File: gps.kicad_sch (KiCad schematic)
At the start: 10 parts, among them J700 Conn_01x02, U700 NEO-6P, X7 Conn_Coaxial

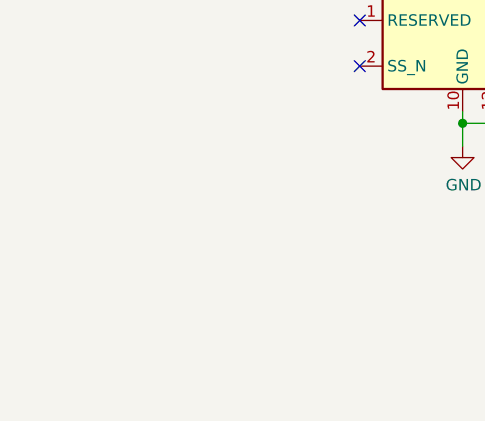
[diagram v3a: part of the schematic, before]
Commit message: Changed the position of the capacitor in the circuit diagram. Capacitors are now close to the components as on the circuit board.
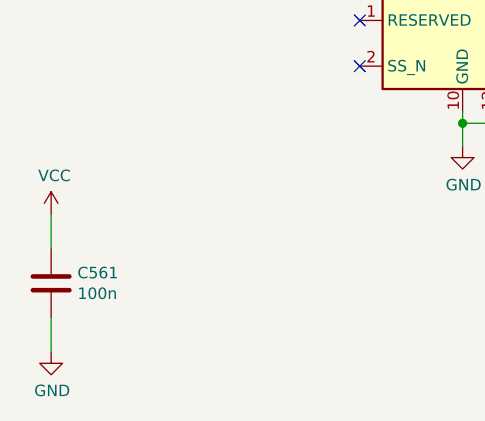
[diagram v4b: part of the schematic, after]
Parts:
- added C561: 100n, Capacitor_SMD:C_0805_2012Metric_Pad1.18x1.45mm_HandSolder, symbol Device:C
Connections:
- net GND: now also C561.2
- net VCC: now also C561.1
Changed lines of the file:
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@@
   (no_connect (at 163.83 91.44))
   (no_connect (at 163.83 101.6))
+  (wire (pts (xy 93.98 121.92) (xy 93.98 125.73))
+    (stroke (width 0) (type solid) (color 0 0 0 0))
+  )
+  (wire (pts (xy 93.98 133.35) (xy 93.98 137.16))
+    (stroke (width 0) (type solid) (color 0 0 0 0))
+  )
   (wire (pts (xy 102.87 80.01) (xy 109.22 80.01))
     (stroke (width 0) (type solid) (color 0 0 0 0))
@@
     )
   )
+  (symbol (lib_id "power:VCC") (at 93.98 121.92 0) (unit 1)
+    (in_bom yes) (on_board yes)
+    (property "Reference" "#PWR0202" (id 0) (at 93.98 125.73 0)
+      (effects (font (size 1.27 1.27)) hide)
+    )
+    (property "Value" "VCC" (id 1) (at 94.3483 117.5956 0))
+    (property "Footprint" "" (id 2) (at 93.98 121.92 0)
+      (effects (font (size 1.27 1.27)) hide)
+    )
+    (property "Datasheet" "" (id 3) (at 93.98 121.92 0)
+      (effects (font (size 1.27 1.27)) hide)
+    )
+    (pin "1")
+  )
   (symbol (lib_id "power:VCC") (at 142.24 60.96 0) (unit 1)
     (in_bom yes) (on_board yes)
@@
     (pin "1")
   )
+  (symbol (lib_id "power:GND") (at 93.98 137.16 0) (unit 1)
+    (in_bom yes) (on_board yes)
+    (property "Reference" "#PWR0201" (id 0) (at 93.98 143.51 0)
+      (effects (font (size 1.27 1.27)) hide)
+    )
+    (property "Value" "GND" (id 1) (at 94.0943 141.4844 0))
+    (property "Footprint" "" (id 2) (at 93.98 137.16 0)
+      (effects (font (size 1.27 1.27)) hide)
+    )
+    (property "Datasheet" "" (id 3) (at 93.98 137.16 0)
+      (effects (font (size 1.27 1.27)) hide)
+    )
+    (pin "1")
+  )
   (symbol (lib_id "power:GND") (at 139.7 114.3 0) (unit 1)
     (in_bom yes) (on_board yes)
@@
       (effects (font (size 1.27 1.27)) hide)
     )
+    (pin "1")
+    (pin "2")
+  )
+  (symbol (lib_id "Device:C") (at 93.98 129.54 0) (unit 1)
+    (in_bom yes) (on_board yes)
+    (property "Reference" "C561" (id 0) (at 96.9011 128.3906 0)
+      (effects (font (size 1.27 1.27)) (justify left))
+    )
+    (property "Value" "100n" (id 1) (at 96.9011 130.6893 0)
+      (effects (font (size 1.27 1.27)) (justify left))
+    )
+    (property "Footprint" "Capacitor_SMD:C_0805_2012Metric_Pad1.18x1.45mm_HandSolder" (id 2) (at 94.9452 133.35 0)
+      (effects (font (size 1.27 1.27)) hide)
+    )
+    (property "Datasheet" "~" (id 3) (at 93.98 129.54 0)
+      (effects (font (size 1.27 1.27)) hide)
+    )
+    (property "JLCBasicPart" "Basic" (id 4) (at 93.98 129.54 0)
+      (effects (font (size 1.27 1.27)) hide)
+    )
+    (property "JLCPartNr" "C49678" (id 5) (at 93.98 129.54 0)
+      (effects (font (size 1.27 1.27)) hide)
+    )
+    (property "JLCType" "CC0805KRX7R9BB104" (id 6) (at 93.98 129.54 0)
+      (effects (font (size 1.27 1.27)) hide)
+    )
+    (property "OriginalType" "FN21X104K500PXG " (id 7) (at 93.98 129.54 0)
+      (effects (font (size 1.27 1.27)) hide)
+    )

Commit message: Progress in PCB. Some changes in Schematis. Solderjumper for modular design added.
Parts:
- X7: footprint muonpi-kicad-library:SMA_Samtec_SMA-J-P-X-ST-EM1_EdgeMount -> muonpi-kicad-library:Connector_Coaxial_SMA_edge_combined
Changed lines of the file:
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@@
       (effects (font (size 1.27 1.27)) (justify left))
     )
-    (property "Footprint" "muonpi-kicad-library:SMA_Samtec_SMA-J-P-X-ST-EM1_EdgeMount" (id 2) (at 176.53 80.01 0)
+    (property "Footprint" "muonpi-kicad-library:Connector_Coaxial_SMA_edge_combined" (id 2) (at 176.53 80.01 0)
       (effects (font (size 1.27 1.27)) hide)
     )

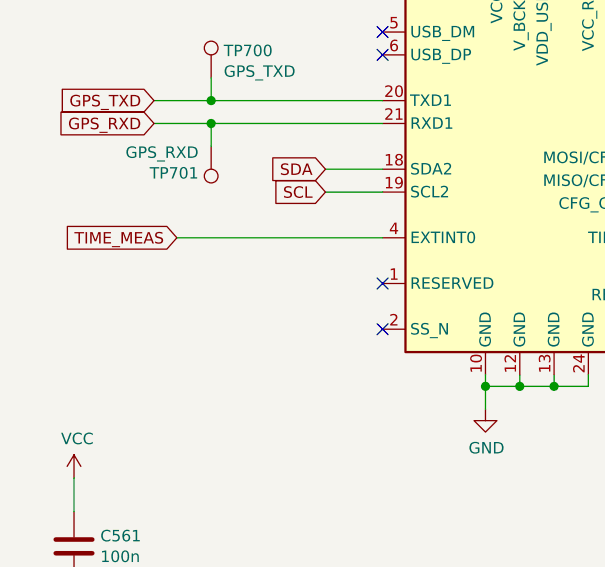
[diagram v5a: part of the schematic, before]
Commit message: Removed optionals parts. Cleaned up Schematics
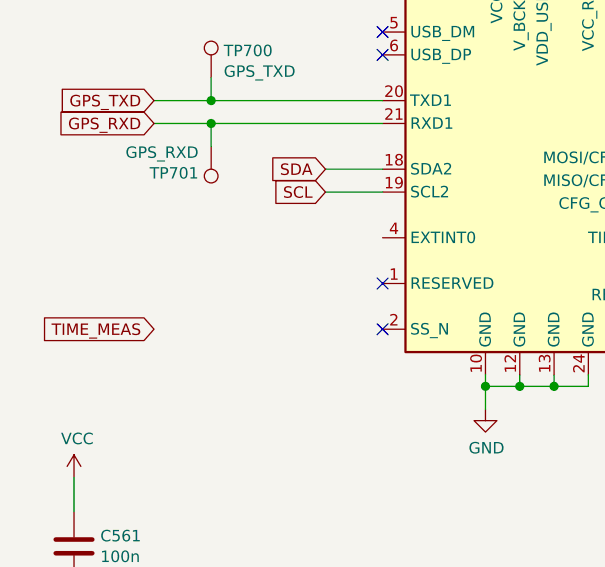
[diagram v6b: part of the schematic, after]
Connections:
- net TIME_MEAS: no longer U700.4 (EXTINT0)
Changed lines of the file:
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@@
-    (stroke (width 0) (type solid) (color 0 0 0 0))
-  )
-  (wire (pts (xy 105.41 95.25) (xy 128.27 95.25))
     (stroke (width 0) (type solid) (color 0 0 0 0))
   )
@@
     )
   )
-  (global_label "TIME_MEAS" (shape input) (at 105.41 95.25 180)
+  (global_label "TIME_MEAS" (shape input) (at 102.87 105.41 180)
     (effects (font (size 1.27 1.27)) (justify right))
-    (property "Intersheet References" "${INTERSHEET_REFS}" (id 0) (at 91.4339 95.1706 0)
+    (property "Intersheet References" "${INTERSHEET_REFS}" (id 0) (at 88.8939 105.3306 0)
       (effects (font (size 1.27 1.27)) (justify right) hide)
     )

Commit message: Rough routing finished
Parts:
- added JP700, JP701, JP702, JP703, JP704, JP705: SolderJumper_2_Bridged, Jumper:SolderJumper-2_P1.3mm_Bridged_Pad1.0x1.5mm, symbol Jumper:SolderJumper_2_Bridged
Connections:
- net GPS_RXD: now also JP701.1 (A); no longer TP701.1, U700.21 (RXD1)
- net GPS_TXD: now also JP700.1 (A); no longer TP700.1, U700.20 (TXD1)
- net SCL: now also JP703.1 (A); no longer U700.19 (SCL2)
- net SDA: now also JP702.1 (A); no longer U700.18 (SDA2)
- net TIMEPULSE: now also JP704.2 (B); no longer R705.2
- net TIME_MEAS: now also JP705.1 (A)
- net at U700.4 (EXTINT0): now also JP705.2 (B)
- new net: JP702.2 (B), U700.18 (SDA2)
- new net: JP703.2 (B), U700.19 (SCL2)
- new net: JP700.2 (B), TP700.1, U700.20 (TXD1)
- new net: JP701.2 (B), TP701.1, U700.21 (RXD1)
- new net TIMEPULSE_LED: JP704.1 (A), R705.2

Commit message: some changes after first test of boards. Package of SN74LV221AD changed to SOIC-16.
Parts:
- C561: JLCplace (none) -> C49678; Supplier (none) -> LCSC
- J700: OriginalType (none) -> 67997-100HLF; Supplier (none) -> Mouser
- JP700, JP701, JP702, JP703, JP704, JP705, TP700, TP701: Supplier (none) -> --
- L700: alternativ supply (none) -> mouser; alternativ supply part nr. (none) -> CE201210-27NJ
- R700: JLCplace (none) -> C17415; Supplier (none) -> LCSC
- R704: JLCplace (none) -> C17477; Supplier (none) -> LCSC
- R705, R706: JLCplace (none) -> C17738; Supplier (none) -> LCSC
- U700: Supplier (none) -> ??
- X7: JLCBasicPart (none) -> Extended; JLCPartNr (none) -> C88374; JLCType (none) -> U.FL-R-SMT-1(80); OriginalType (none) -> U.FL-R-SMT-1(80); Supplier (none) -> LCSC
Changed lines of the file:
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@@
+      (effects (font (size 1.27 1.27)) hide)
+    )
+    (property "Supplier" "--" (id 4) (at 109.22 77.47 0)
       (effects (font (size 1.27 1.27)) hide)
     )
@@
     )
     (property "Datasheet" "~" (id 3) (at 104.14 85.09 0)
+      (effects (font (size 1.27 1.27)) hide)
+    )
+    (property "Supplier" "--" (id 4) (at 109.22 85.09 0)
       (effects (font (size 1.27 1.27)) hide)
     )
@@
       (effects (font (size 1.27 1.27)) hide)
     )
+    (property "alternativ supply" "mouser" (id 9) (at 170.18 74.93 0)
+      (effects (font (size 1.27 1.27)) hide)
+    )
+    (property "alternativ supply part nr." "CE201210-27NJ" (id 10) (at 170.18 74.93 0)
+      (effects (font (size 1.27 1.27)) hide)
+    )
     (pin "1")
     (pin "2")
@@
       (effects (font (size 1.27 1.27)) hide)
     )
+    (property "Supplier" "--" (id 4) (at 102.87 80.01 0)
+      (effects (font (size 1.27 1.27)) hide)
+    )
     (pin "1")
     (pin "2")
@@
       (effects (font (size 1.27 1.27)) hide)
     )
+    (property "Supplier" "--" (id 4) (at 102.87 82.55 0)
+      (effects (font (size 1.27 1.27)) hide)
+    )
     (pin "1")
     (pin "2")
@@
       (effects (font (size 1.27 1.27)) hide)
     )
+    (property "Supplier" "--" (id 4) (at 120.65 97.79 0)
+      (effects (font (size 1.27 1.27)) hide)
+    )
     (pin "1")
     (pin "2")
@@
       (effects (font (size 1.27 1.27)) hide)
     )
+    (property "Supplier" "--" (id 4) (at 123.19 87.63 0)
+      (effects (font (size 1.27 1.27)) hide)
+    )
     (pin "1")
     (pin "2")
@@
       (effects (font (size 1.27 1.27)) hide)
     )
+    (property "Supplier" "--" (id 4) (at 123.19 90.17 0)
+      (effects (font (size 1.27 1.27)) hide)
+    )
     (pin "1")
     (pin "2")
@@
       (effects (font (size 1.27 1.27)) hide)
     )
+    (property "Supplier" "--" (id 4) (at 222.25 95.25 0)
+      (effects (font (size 1.27 1.27)) hide)
+    )
     (pin "1")
     (pin "2")
@@
       (effects (font (size 1.27 1.27)) hide)
     )
+    (property "Supplier" "LCSC" (id 8) (at 154.94 59.69 0)
+      (effects (font (size 1.27 1.27)) hide)
+    )
+    (property "JLCplace" "C17477" (id 9) (at 154.94 59.69 0)
+      (effects (font (size 1.27 1.27)) hide)
+    )
     (pin "1")
     (pin "2")
@@
     )
     (property "OriginalType" "RK73H2ATTD10R0F " (id 7) (at 170.18 66.04 0)
+      (effects (font (size 1.27 1.27)) hide)
+    )
+    (property "Supplier" "LCSC" (id 8) (at 170.18 66.04 0)
+      (effects (font (size 1.27 1.27)) hide)
+    )
+    (property "JLCplace" "C17415" (id 9) (at 170.18 66.04 0)
       (effects (font (size 1.27 1.27)) hide)
     )
@@
       (effects (font (size 1.27 1.27)) hide)
     )
+    (property "Supplier" "LCSC" (id 8) (at 208.28 85.09 0)
+      (effects (font (size 1.27 1.27)) hide)
+    )
+    (property "JLCplace" "C17738" (id 9) (at 208.28 85.09 0)
+      (effects (font (size 1.27 1.27)) hide)
+    )
     (pin "1")
     (pin "2")
@@
       (effects (font (size 1.27 1.27)) hide)
     )
+    (property "Supplier" "LCSC" (id 8) (at 208.28 95.25 0)
+      (effects (font (size 1.27 1.27)) hide)
+    )
+    (property "JLCplace" "C17738" (id 9) (at 208.28 95.25 0)
+      (effects (font (size 1.27 1.27)) hide)
+    )
     (pin "1")
     (pin "2")
@@
       (effects (font (size 1.27 1.27)) hide)
     )
+    (property "OriginalType" "67997-100HLF" (id 4) (at 222.25 82.55 0)
+      (effects (font (size 1.27 1.27)) hide)
+    )
+    (property "Supplier" "Mouser" (id 5) (at 222.25 82.55 0)
+      (effects (font (size 1.27 1.27)) hide)
+    )
     (pin "1")
     (pin "2")
@@
       (effects (font (size 1.27 1.27)) hide)
     )
+    (property "Supplier" "LCSC" (id 8) (at 93.98 129.54 0)
+      (effects (font (size 1.27 1.27)) hide)
+    )
+    (property "JLCplace" "C49678" (id 9) (at 93.98 129.54 0)
+      (effects (font (size 1.27 1.27)) hide)
+    )
     (pin "1")
     (pin "2")
@@
     )
     (property "Datasheet" " ~" (id 3) (at 176.53 80.01 0)
+      (effects (font (size 1.27 1.27)) hide)
+    )
+    (property "JLCBasicPart" "Extended" (id 4) (at 176.53 80.01 0)
+      (effects (font (size 1.27 1.27)) hide)
+    )
+    (property "JLCPartNr" "C88374" (id 5) (at 176.53 80.01 0)
+      (effects (font (size 1.27 1.27)) hide)
+    )
+    (property "JLCType" "U.FL-R-SMT-1(80)" (id 6) (at 176.53 80.01 0)
+      (effects (font (size 1.27 1.27)) hide)
+    )
+    (property "OriginalType" "U.FL-R-SMT-1(80)" (id 7) (at 176.53 80.01 0)
+      (effects (font (size 1.27 1.27)) hide)
+    )
+    (property "Supplier" "LCSC" (id 8) (at 176.53 80.01 0)
       (effects (font (size 1.27 1.27)) hide)
     )
@@
       (effects (font (size 1.27 1.27)) hide)
     )
+    (property "Supplier" "??" (id 4) (at 146.05 87.63 0)
+      (effects (font (size 1.27 1.27)) hide)
+    )
